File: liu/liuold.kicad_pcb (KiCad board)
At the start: 2 copper layers, 96.5 x 66 mm, 20 parts, among them J1 Screw Termial, J2 Screw Terminal, J3 Screw Termial, J4 Screw Termial, J5 I2C, J6 RotaryEncoder, U1 VoltageRegulator, U2 ESP32, U3 TJA1050

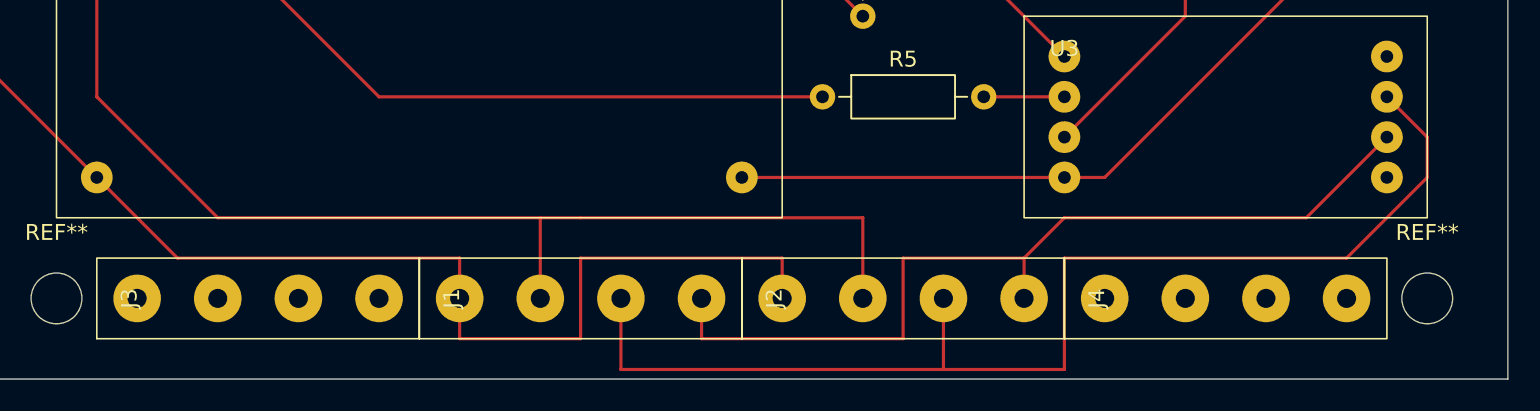
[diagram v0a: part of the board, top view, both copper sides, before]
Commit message: 4 screw terminals
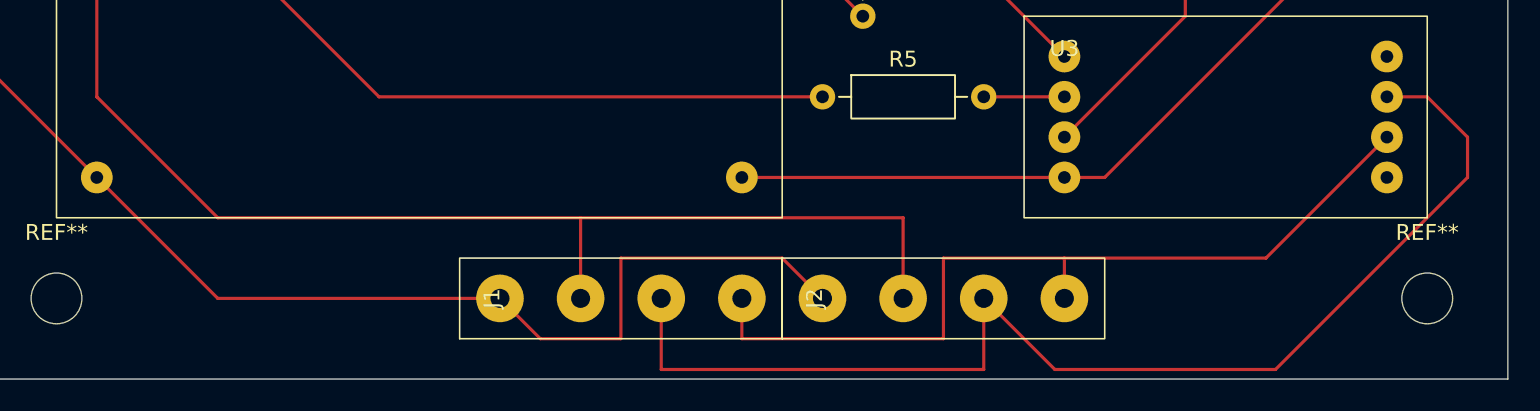
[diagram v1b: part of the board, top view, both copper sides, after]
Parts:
- removed J3, J4: Screw Termial, Peabrain:ScrewTerminals_4P
- moved J1 2.54 mm to (58.4, 86.4)
- moved J2 2.54 mm to (78.7, 86.4)
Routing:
- net /12V: track 74.3 -> 76.8 mm
- net /CANL: track 56.5 -> 54.0 mm
- net /GND: track 245.2 -> 243.3 mm
